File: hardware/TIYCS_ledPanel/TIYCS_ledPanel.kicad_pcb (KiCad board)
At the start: 2 copper layers, 203 x 203 mm, 120 parts

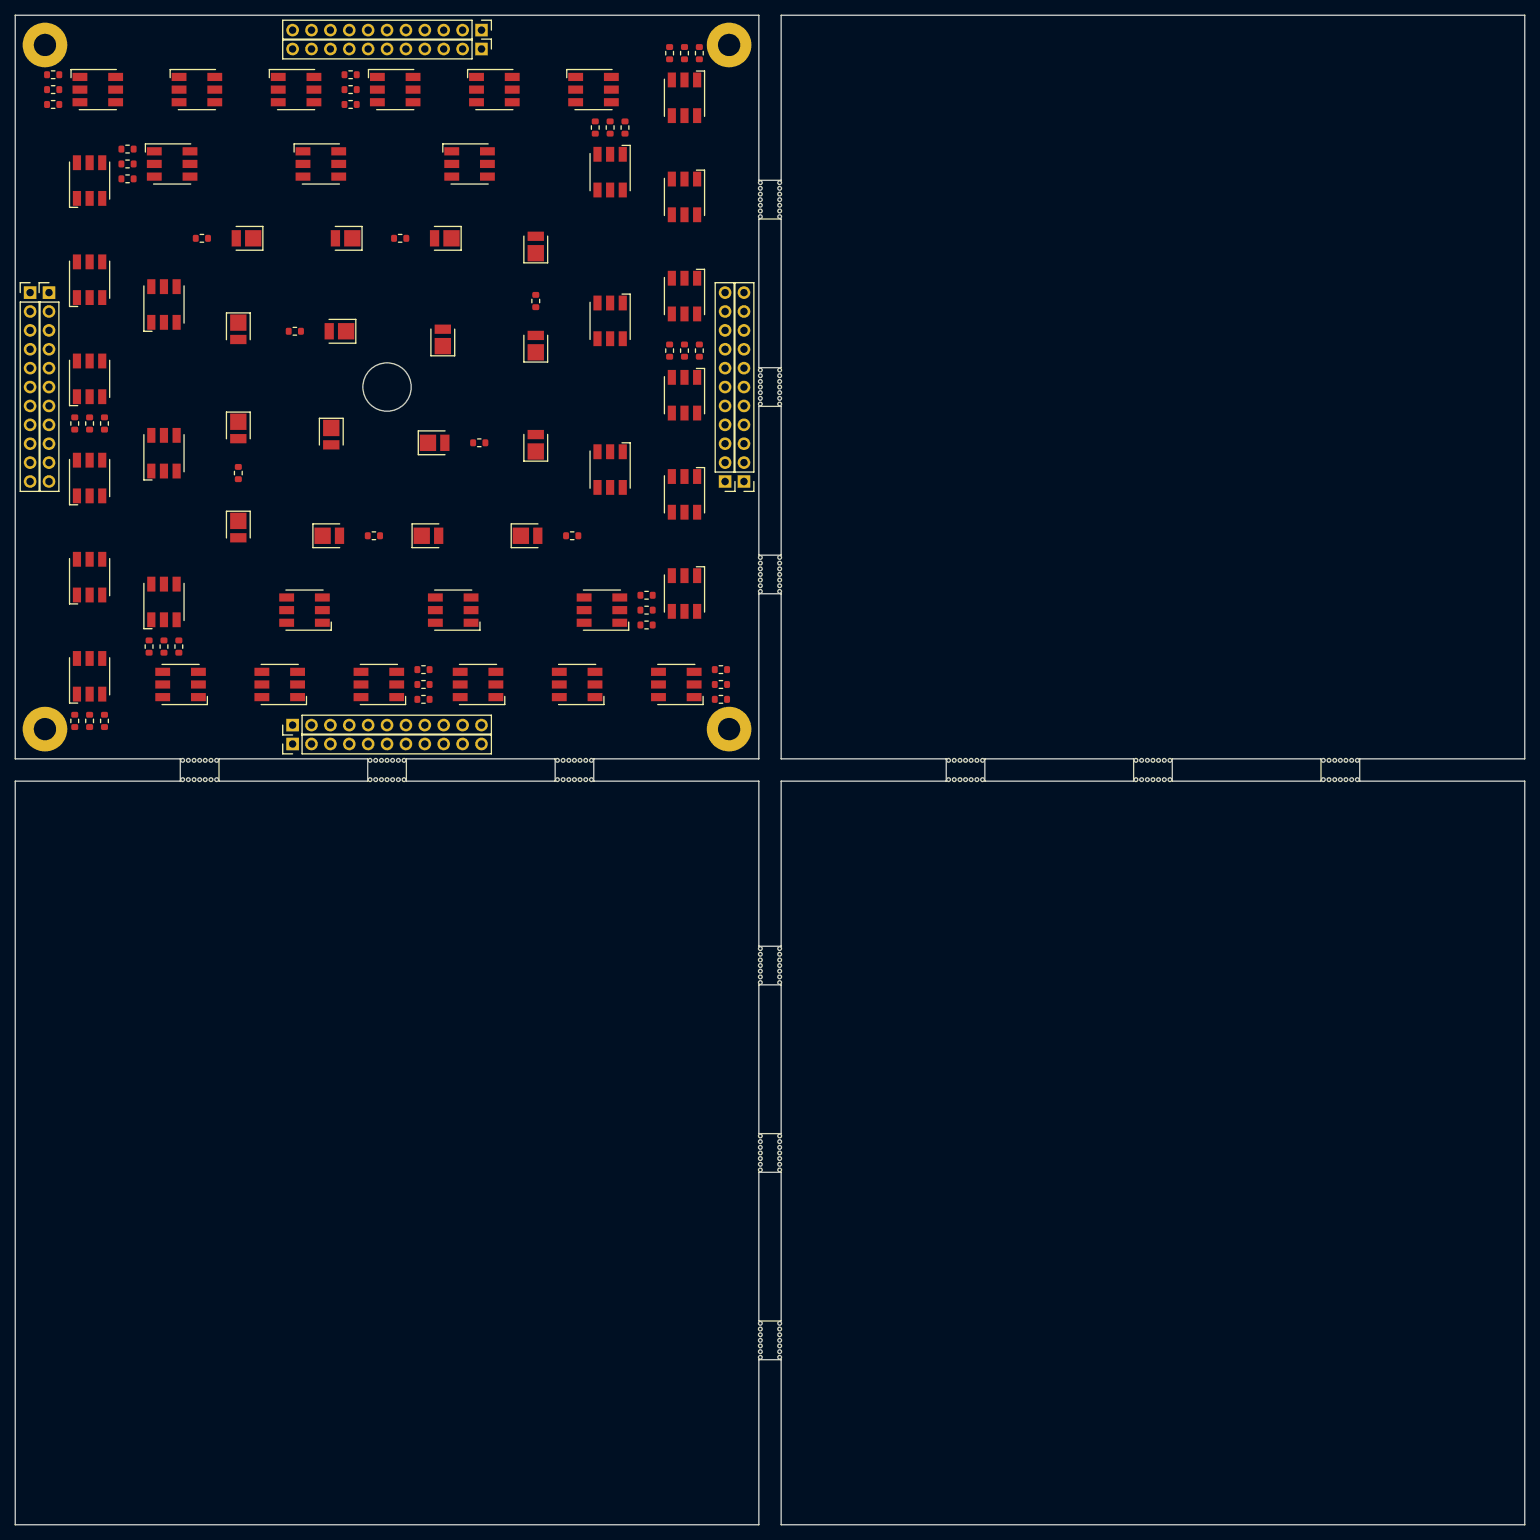
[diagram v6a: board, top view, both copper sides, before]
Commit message: PCLL-2 routed
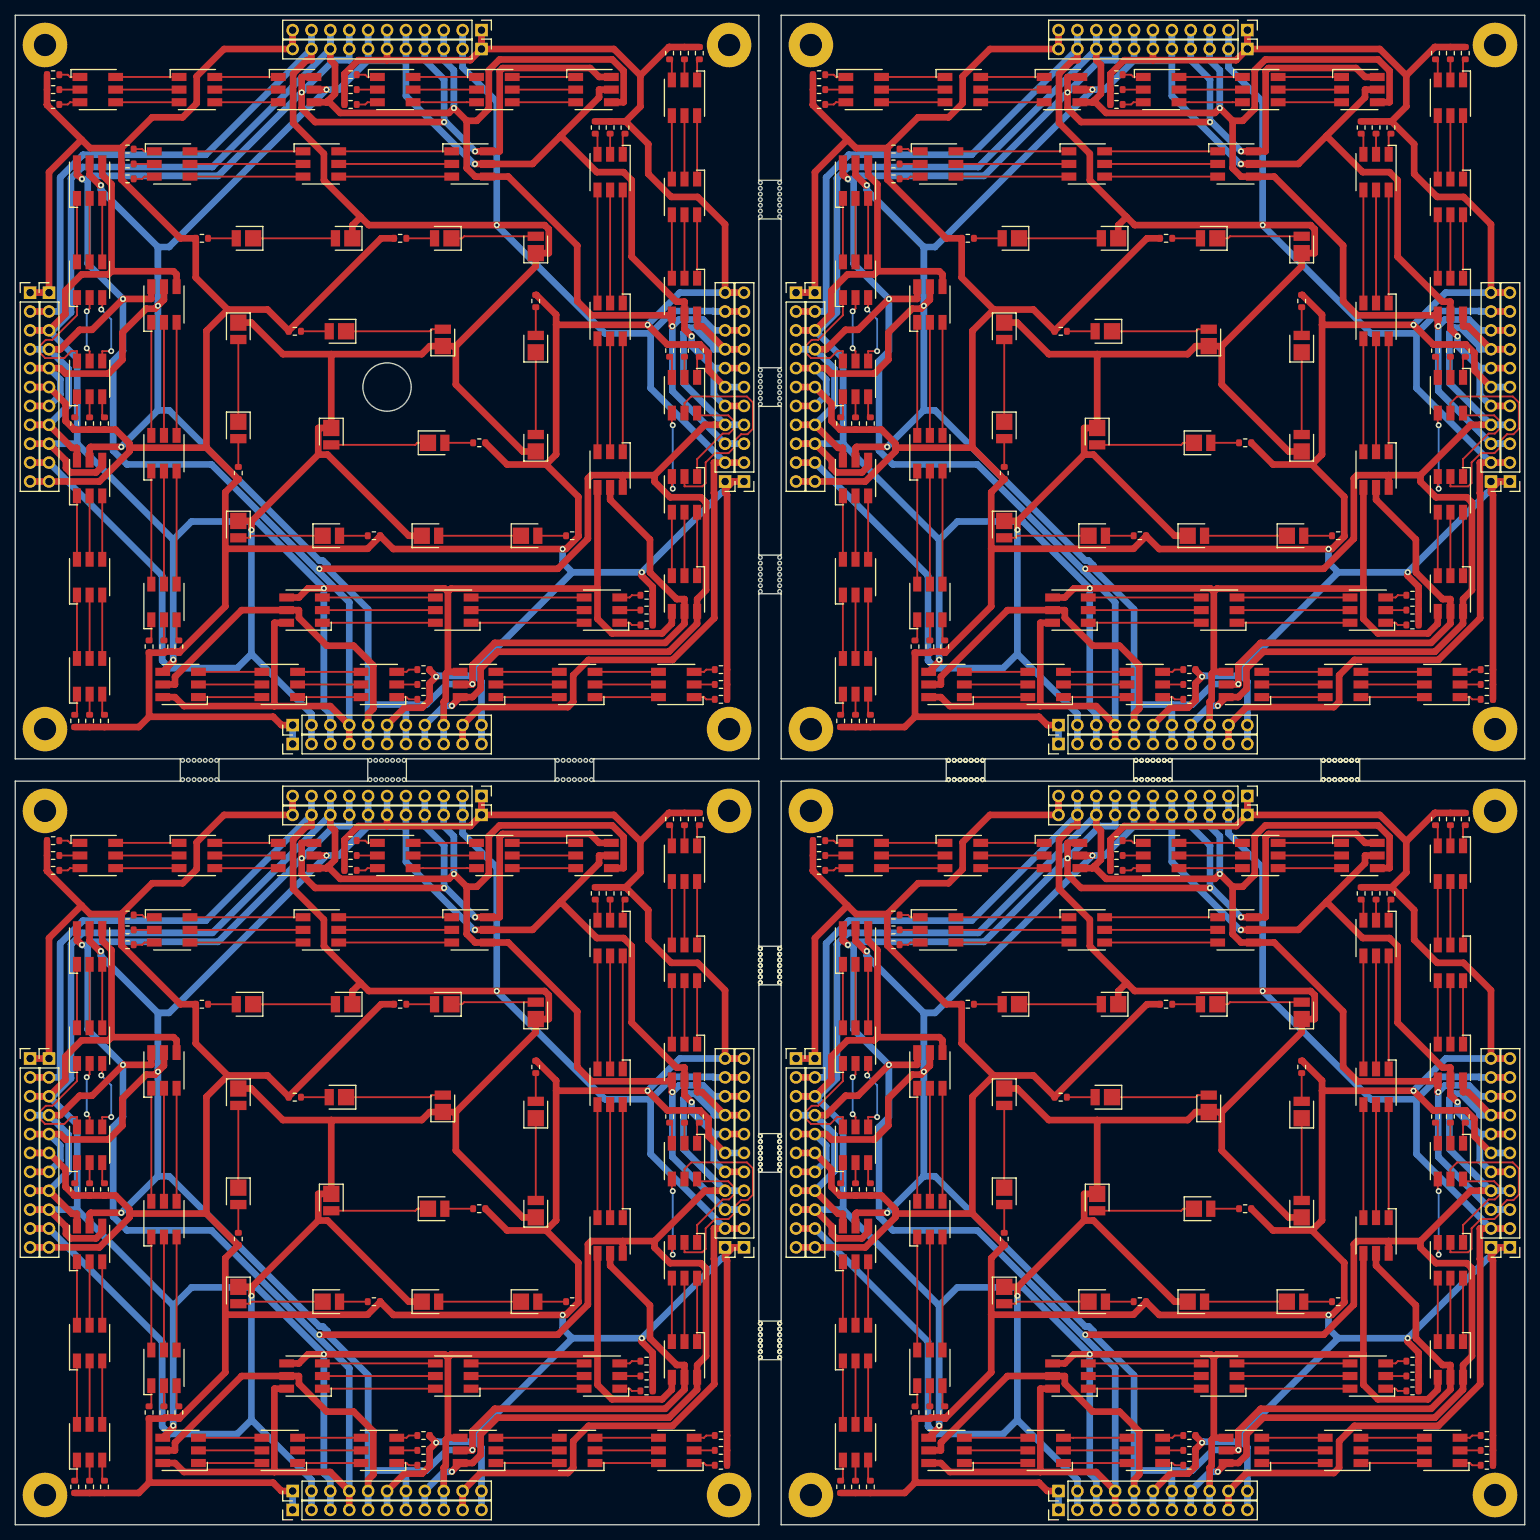
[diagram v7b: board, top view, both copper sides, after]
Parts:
- added H_10: MountingHole_3mm_Pad, MountingHole_3mm_Pad, F.Cu at (46.0, 149.0)
- added H_11: MountingHole_3mm_Pad, MountingHole_3mm_Pad, F.Cu at (-46.0, 149.0)
- added H_12: MountingHole_3mm_Pad, MountingHole_3mm_Pad, F.Cu at (57.0, 57.0)
- added H_13: MountingHole_3mm_Pad, MountingHole_3mm_Pad, F.Cu at (149.0, 57.0)
- added H_14: MountingHole_3mm_Pad, MountingHole_3mm_Pad, F.Cu at (149.0, 149.0)
- added H_15: MountingHole_3mm_Pad, MountingHole_3mm_Pad, F.Cu at (57.0, 149.0)
- added H_4: MountingHole_3mm_Pad, MountingHole_3mm_Pad, F.Cu at (57.0, -46.0)
- added H_5: MountingHole_3mm_Pad, MountingHole_3mm_Pad, F.Cu at (149.0, -46.0)
- added H_6: MountingHole_3mm_Pad, MountingHole_3mm_Pad, F.Cu at (149.0, 46.0)
- added H_7: MountingHole_3mm_Pad, MountingHole_3mm_Pad, F.Cu at (57.0, 46.0)
- added H_8: MountingHole_3mm_Pad, MountingHole_3mm_Pad, F.Cu at (-46.0, 57.0)
- added H_9: MountingHole_3mm_Pad, MountingHole_3mm_Pad, F.Cu at (46.0, 57.0)
- added LED_RGB2_12: LED_RGB_5050-6, LED_RGB_5050-6, F.Cu at (74.1, -30.0)
- added LED_RGB2_13: LED_RGB_5050-6, LED_RGB_5050-6, F.Cu at (94.1, -30.0)
- added LED_RGB2_14: LED_RGB_5050-6, LED_RGB_5050-6, F.Cu at (114.1, -30.0)
- added LED_RGB2_15: LED_RGB_5050-6, LED_RGB_5050-6, F.Cu at (133.0, -28.9)
- added LED_RGB2_16: LED_RGB_5050-6, LED_RGB_5050-6, F.Cu at (133.0, -8.90)
- added LED_RGB2_17: LED_RGB_5050-6, LED_RGB_5050-6, F.Cu at (133.0, 11.1)
- added LED_RGB2_18: LED_RGB_5050-6, LED_RGB_5050-6, F.Cu at (131.9, 30.0)
- added LED_RGB2_19: LED_RGB_5050-6, LED_RGB_5050-6, F.Cu at (111.9, 30.0)
- added LED_RGB2_20: LED_RGB_5050-6, LED_RGB_5050-6, F.Cu at (91.9, 30.0)
- added LED_RGB2_21: LED_RGB_5050-6, LED_RGB_5050-6, F.Cu at (73.0, 28.9)
- added LED_RGB2_22: LED_RGB_5050-6, LED_RGB_5050-6, F.Cu at (73.0, 8.90)
- added LED_RGB2_23: LED_RGB_5050-6, LED_RGB_5050-6, F.Cu at (73.0, -11.1)
- added LED_RGB2_24: LED_RGB_5050-6, LED_RGB_5050-6, F.Cu at (-28.9, 73.0)
- added LED_RGB2_25: LED_RGB_5050-6, LED_RGB_5050-6, F.Cu at (-8.90, 73.0)
- added LED_RGB2_26: LED_RGB_5050-6, LED_RGB_5050-6, F.Cu at (11.1, 73.0)
- added LED_RGB2_27: LED_RGB_5050-6, LED_RGB_5050-6, F.Cu at (30.0, 74.1)
- added LED_RGB2_28: LED_RGB_5050-6, LED_RGB_5050-6, F.Cu at (30.0, 94.1)
- added LED_RGB2_29: LED_RGB_5050-6, LED_RGB_5050-6, F.Cu at (30.0, 114.1)
- added LED_RGB2_30: LED_RGB_5050-6, LED_RGB_5050-6, F.Cu at (28.9, 133.0)
- added LED_RGB2_31: LED_RGB_5050-6, LED_RGB_5050-6, F.Cu at (8.90, 133.0)
- added LED_RGB2_32: LED_RGB_5050-6, LED_RGB_5050-6, F.Cu at (-11.1, 133.0)
- added LED_RGB2_33: LED_RGB_5050-6, LED_RGB_5050-6, F.Cu at (-30.0, 131.9)
- added LED_RGB2_34: LED_RGB_5050-6, LED_RGB_5050-6, F.Cu at (-30.0, 111.9)
- added LED_RGB2_35: LED_RGB_5050-6, LED_RGB_5050-6, F.Cu at (-30.0, 91.9)
- added LED_RGB2_36: LED_RGB_5050-6, LED_RGB_5050-6, F.Cu at (74.1, 73.0)
- added LED_RGB2_37: LED_RGB_5050-6, LED_RGB_5050-6, F.Cu at (94.1, 73.0)
- added LED_RGB2_38: LED_RGB_5050-6, LED_RGB_5050-6, F.Cu at (114.1, 73.0)
- added LED_RGB2_39: LED_RGB_5050-6, LED_RGB_5050-6, F.Cu at (133.0, 74.1)
- added LED_RGB2_40: LED_RGB_5050-6, LED_RGB_5050-6, F.Cu at (133.0, 94.1)
- added LED_RGB2_41: LED_RGB_5050-6, LED_RGB_5050-6, F.Cu at (133.0, 114.1)
- added LED_RGB2_42: LED_RGB_5050-6, LED_RGB_5050-6, F.Cu at (131.9, 133.0)
- added LED_RGB2_43: LED_RGB_5050-6, LED_RGB_5050-6, F.Cu at (111.9, 133.0)
- added LED_RGB2_44: LED_RGB_5050-6, LED_RGB_5050-6, F.Cu at (91.9, 133.0)
- added LED_RGB2_45: LED_RGB_5050-6, LED_RGB_5050-6, F.Cu at (73.0, 131.9)
- added LED_RGB2_46: LED_RGB_5050-6, LED_RGB_5050-6, F.Cu at (73.0, 111.9)
- added LED_RGB2_47: LED_RGB_5050-6, LED_RGB_5050-6, F.Cu at (73.0, 91.9)
- added LED_RGB_24: LED_RGB_5050-6, LED_RGB_5050-6, F.Cu at (64.1, -40.0)
- added LED_RGB_25: LED_RGB_5050-6, LED_RGB_5050-6, F.Cu at (77.4, -40.0)
- added LED_RGB_26: LED_RGB_5050-6, LED_RGB_5050-6, F.Cu at (90.8, -40.0)
- added LED_RGB_27: LED_RGB_5050-6, LED_RGB_5050-6, F.Cu at (104.1, -40.0)
- added LED_RGB_28: LED_RGB_5050-6, LED_RGB_5050-6, F.Cu at (117.4, -40.0)
- added LED_RGB_29: LED_RGB_5050-6, LED_RGB_5050-6, F.Cu at (130.8, -40.0)
- added LED_RGB_30: LED_RGB_5050-6, LED_RGB_5050-6, F.Cu at (143.0, -38.9)
- added LED_RGB_31: LED_RGB_5050-6, LED_RGB_5050-6, F.Cu at (143.0, -25.6)
- added LED_RGB_32: LED_RGB_5050-6, LED_RGB_5050-6, F.Cu at (143.0, -12.2)
- added LED_RGB_33: LED_RGB_5050-6, LED_RGB_5050-6, F.Cu at (143.0, 1.10)
- added LED_RGB_34: LED_RGB_5050-6, LED_RGB_5050-6, F.Cu at (143.0, 14.4)
- added LED_RGB_35: LED_RGB_5050-6, LED_RGB_5050-6, F.Cu at (143.0, 27.8)
- added LED_RGB_36: LED_RGB_5050-6, LED_RGB_5050-6, F.Cu at (141.9, 40.0)
- added LED_RGB_37: LED_RGB_5050-6, LED_RGB_5050-6, F.Cu at (128.6, 40.0)
- added LED_RGB_38: LED_RGB_5050-6, LED_RGB_5050-6, F.Cu at (115.2, 40.0)
- added LED_RGB_39: LED_RGB_5050-6, LED_RGB_5050-6, F.Cu at (101.9, 40.0)
- added LED_RGB_40: LED_RGB_5050-6, LED_RGB_5050-6, F.Cu at (88.6, 40.0)
- added LED_RGB_41: LED_RGB_5050-6, LED_RGB_5050-6, F.Cu at (75.2, 40.0)
- added LED_RGB_42: LED_RGB_5050-6, LED_RGB_5050-6, F.Cu at (63.0, 38.9)
- added LED_RGB_43: LED_RGB_5050-6, LED_RGB_5050-6, F.Cu at (63.0, 25.6)
- added LED_RGB_44: LED_RGB_5050-6, LED_RGB_5050-6, F.Cu at (63.0, 12.2)
- added LED_RGB_45: LED_RGB_5050-6, LED_RGB_5050-6, F.Cu at (63.0, -1.10)
- added LED_RGB_46: LED_RGB_5050-6, LED_RGB_5050-6, F.Cu at (63.0, -14.4)
- added LED_RGB_47: LED_RGB_5050-6, LED_RGB_5050-6, F.Cu at (63.0, -27.8)
- added LED_RGB_48: LED_RGB_5050-6, LED_RGB_5050-6, F.Cu at (-38.9, 63.0)
- added LED_RGB_49: LED_RGB_5050-6, LED_RGB_5050-6, F.Cu at (-25.6, 63.0)
- added LED_RGB_50: LED_RGB_5050-6, LED_RGB_5050-6, F.Cu at (-12.2, 63.0)
- added LED_RGB_51: LED_RGB_5050-6, LED_RGB_5050-6, F.Cu at (1.10, 63.0)
- added LED_RGB_52: LED_RGB_5050-6, LED_RGB_5050-6, F.Cu at (14.4, 63.0)
- added LED_RGB_53: LED_RGB_5050-6, LED_RGB_5050-6, F.Cu at (27.8, 63.0)
- added LED_RGB_54: LED_RGB_5050-6, LED_RGB_5050-6, F.Cu at (40.0, 64.1)
- added LED_RGB_55: LED_RGB_5050-6, LED_RGB_5050-6, F.Cu at (40.0, 77.4)
- added LED_RGB_56: LED_RGB_5050-6, LED_RGB_5050-6, F.Cu at (40.0, 90.8)
- added LED_RGB_57: LED_RGB_5050-6, LED_RGB_5050-6, F.Cu at (40.0, 104.1)
- added LED_RGB_58: LED_RGB_5050-6, LED_RGB_5050-6, F.Cu at (40.0, 117.4)
- added LED_RGB_59: LED_RGB_5050-6, LED_RGB_5050-6, F.Cu at (40.0, 130.8)
- added LED_RGB_60: LED_RGB_5050-6, LED_RGB_5050-6, F.Cu at (38.9, 143.0)
- added LED_RGB_61: LED_RGB_5050-6, LED_RGB_5050-6, F.Cu at (25.6, 143.0)
- added LED_RGB_62: LED_RGB_5050-6, LED_RGB_5050-6, F.Cu at (12.2, 143.0)
- added LED_RGB_63: LED_RGB_5050-6, LED_RGB_5050-6, F.Cu at (-1.10, 143.0)
- added LED_RGB_64: LED_RGB_5050-6, LED_RGB_5050-6, F.Cu at (-14.4, 143.0)
- added LED_RGB_65: LED_RGB_5050-6, LED_RGB_5050-6, F.Cu at (-27.8, 143.0)
- added LED_RGB_66: LED_RGB_5050-6, LED_RGB_5050-6, F.Cu at (-40.0, 141.9)
- added LED_RGB_67: LED_RGB_5050-6, LED_RGB_5050-6, F.Cu at (-40.0, 128.6)
- added LED_RGB_68: LED_RGB_5050-6, LED_RGB_5050-6, F.Cu at (-40.0, 115.2)
- added LED_RGB_69: LED_RGB_5050-6, LED_RGB_5050-6, F.Cu at (-40.0, 101.9)
- added LED_RGB_70: LED_RGB_5050-6, LED_RGB_5050-6, F.Cu at (-40.0, 88.6)
- added LED_RGB_71: LED_RGB_5050-6, LED_RGB_5050-6, F.Cu at (-40.0, 75.2)
- added LED_RGB_72: LED_RGB_5050-6, LED_RGB_5050-6, F.Cu at (64.1, 63.0)
- added LED_RGB_73: LED_RGB_5050-6, LED_RGB_5050-6, F.Cu at (77.4, 63.0)
- added LED_RGB_74: LED_RGB_5050-6, LED_RGB_5050-6, F.Cu at (90.8, 63.0)
- added LED_RGB_75: LED_RGB_5050-6, LED_RGB_5050-6, F.Cu at (104.1, 63.0)
- added LED_RGB_76: LED_RGB_5050-6, LED_RGB_5050-6, F.Cu at (117.4, 63.0)
- added LED_RGB_77: LED_RGB_5050-6, LED_RGB_5050-6, F.Cu at (130.8, 63.0)
- added LED_RGB_78: LED_RGB_5050-6, LED_RGB_5050-6, F.Cu at (143.0, 64.1)
- added LED_RGB_79: LED_RGB_5050-6, LED_RGB_5050-6, F.Cu at (143.0, 77.4)
- added LED_RGB_80: LED_RGB_5050-6, LED_RGB_5050-6, F.Cu at (143.0, 90.8)
- added LED_RGB_81: LED_RGB_5050-6, LED_RGB_5050-6, F.Cu at (143.0, 104.1)
- added LED_RGB_82: LED_RGB_5050-6, LED_RGB_5050-6, F.Cu at (143.0, 117.4)
- added LED_RGB_83: LED_RGB_5050-6, LED_RGB_5050-6, F.Cu at (143.0, 130.8)
- added LED_RGB_84: LED_RGB_5050-6, LED_RGB_5050-6, F.Cu at (141.9, 143.0)
- added LED_RGB_85: LED_RGB_5050-6, LED_RGB_5050-6, F.Cu at (128.6, 143.0)
- added LED_RGB_86: LED_RGB_5050-6, LED_RGB_5050-6, F.Cu at (115.2, 143.0)
- added LED_RGB_87: LED_RGB_5050-6, LED_RGB_5050-6, F.Cu at (101.9, 143.0)
- added LED_RGB_88: LED_RGB_5050-6, LED_RGB_5050-6, F.Cu at (88.6, 143.0)
- added LED_RGB_89: LED_RGB_5050-6, LED_RGB_5050-6, F.Cu at (75.2, 143.0)
- added LED_RGB_90: LED_RGB_5050-6, LED_RGB_5050-6, F.Cu at (63.0, 141.9)
- added LED_RGB_91: LED_RGB_5050-6, LED_RGB_5050-6, F.Cu at (63.0, 128.6)
- added LED_RGB_92: LED_RGB_5050-6, LED_RGB_5050-6, F.Cu at (63.0, 115.2)
- added LED_RGB_93: LED_RGB_5050-6, LED_RGB_5050-6, F.Cu at (63.0, 101.9)
- added LED_RGB_94: LED_RGB_5050-6, LED_RGB_5050-6, F.Cu at (63.0, 88.6)
- added LED_RGB_95: LED_RGB_5050-6, LED_RGB_5050-6, F.Cu at (63.0, 75.2)
- added LED_W2_10: LED_PLCC_2835, LED_PLCC_2835, F.Cu at (6.40, 110.5)
- added LED_W2_11: LED_PLCC_2835, LED_PLCC_2835, F.Cu at (-7.50, 109.4)
- added LED_W2_12: LED_PLCC_2835, LED_PLCC_2835, F.Cu at (96.6, 95.5)
- added LED_W2_13: LED_PLCC_2835, LED_PLCC_2835, F.Cu at (110.5, 96.6)
- added LED_W2_14: LED_PLCC_2835, LED_PLCC_2835, F.Cu at (109.4, 110.5)
- added LED_W2_15: LED_PLCC_2835, LED_PLCC_2835, F.Cu at (95.5, 109.4)
- added LED_W2_4: LED_PLCC_2835, LED_PLCC_2835, F.Cu at (96.6, -7.50)
- added LED_W2_5: LED_PLCC_2835, LED_PLCC_2835, F.Cu at (110.5, -6.40)
- added LED_W2_6: LED_PLCC_2835, LED_PLCC_2835, F.Cu at (109.4, 7.50)
- added LED_W2_7: LED_PLCC_2835, LED_PLCC_2835, F.Cu at (95.5, 6.40)
- added LED_W2_8: LED_PLCC_2835, LED_PLCC_2835, F.Cu at (-6.40, 95.5)
- added LED_W2_9: LED_PLCC_2835, LED_PLCC_2835, F.Cu at (7.50, 96.6)
- added LED_W_12: LED_PLCC_2835, LED_PLCC_2835, F.Cu at (84.1, -20.0)
- added LED_W_13: LED_PLCC_2835, LED_PLCC_2835, F.Cu at (97.4, -20.0)
- added LED_W_14: LED_PLCC_2835, LED_PLCC_2835, F.Cu at (110.8, -20.0)
- added LED_W_15: LED_PLCC_2835, LED_PLCC_2835, F.Cu at (123.0, -18.9)
- added LED_W_16: LED_PLCC_2835, LED_PLCC_2835, F.Cu at (123.0, -5.57)
- added LED_W_17: LED_PLCC_2835, LED_PLCC_2835, F.Cu at (123.0, 7.77)
- added LED_W_18: LED_PLCC_2835, LED_PLCC_2835, F.Cu at (121.9, 20.0)
- added LED_W_19: LED_PLCC_2835, LED_PLCC_2835, F.Cu at (108.6, 20.0)
- added LED_W_20: LED_PLCC_2835, LED_PLCC_2835, F.Cu at (95.2, 20.0)
- added LED_W_21: LED_PLCC_2835, LED_PLCC_2835, F.Cu at (83.0, 18.9)
- added LED_W_22: LED_PLCC_2835, LED_PLCC_2835, F.Cu at (83.0, 5.57)
- added LED_W_23: LED_PLCC_2835, LED_PLCC_2835, F.Cu at (83.0, -7.77)
- added LED_W_24: LED_PLCC_2835, LED_PLCC_2835, F.Cu at (-18.9, 83.0)
- added LED_W_25: LED_PLCC_2835, LED_PLCC_2835, F.Cu at (-5.57, 83.0)
- added LED_W_26: LED_PLCC_2835, LED_PLCC_2835, F.Cu at (7.77, 83.0)
- added LED_W_27: LED_PLCC_2835, LED_PLCC_2835, F.Cu at (20.0, 84.1)
- added LED_W_28: LED_PLCC_2835, LED_PLCC_2835, F.Cu at (20.0, 97.4)
- added LED_W_29: LED_PLCC_2835, LED_PLCC_2835, F.Cu at (20.0, 110.8)
- added LED_W_30: LED_PLCC_2835, LED_PLCC_2835, F.Cu at (18.9, 123.0)
- added LED_W_31: LED_PLCC_2835, LED_PLCC_2835, F.Cu at (5.57, 123.0)
- added LED_W_32: LED_PLCC_2835, LED_PLCC_2835, F.Cu at (-7.77, 123.0)
- added LED_W_33: LED_PLCC_2835, LED_PLCC_2835, F.Cu at (-20.0, 121.9)
- added LED_W_34: LED_PLCC_2835, LED_PLCC_2835, F.Cu at (-20.0, 108.6)
- added LED_W_35: LED_PLCC_2835, LED_PLCC_2835, F.Cu at (-20.0, 95.2)
- added LED_W_36: LED_PLCC_2835, LED_PLCC_2835, F.Cu at (84.1, 83.0)
- added LED_W_37: LED_PLCC_2835, LED_PLCC_2835, F.Cu at (97.4, 83.0)
- added LED_W_38: LED_PLCC_2835, LED_PLCC_2835, F.Cu at (110.8, 83.0)
- added LED_W_39: LED_PLCC_2835, LED_PLCC_2835, F.Cu at (123.0, 84.1)
- added LED_W_40: LED_PLCC_2835, LED_PLCC_2835, F.Cu at (123.0, 97.4)
- added LED_W_41: LED_PLCC_2835, LED_PLCC_2835, F.Cu at (123.0, 110.8)
- added LED_W_42: LED_PLCC_2835, LED_PLCC_2835, F.Cu at (121.9, 123.0)
- added LED_W_43: LED_PLCC_2835, LED_PLCC_2835, F.Cu at (108.6, 123.0)
- added LED_W_44: LED_PLCC_2835, LED_PLCC_2835, F.Cu at (95.2, 123.0)
- added LED_W_45: LED_PLCC_2835, LED_PLCC_2835, F.Cu at (83.0, 121.9)
- added LED_W_46: LED_PLCC_2835, LED_PLCC_2835, F.Cu at (83.0, 108.6)
- added LED_W_47: LED_PLCC_2835, LED_PLCC_2835, F.Cu at (83.0, 95.2)
- added R_0_0_RGB1: R_0603_1608Metric, R_0603_1608Metric, F.Cu at (58.1, -40.0)
- added R_0_0_RGB3: R_0603_1608Metric, R_0603_1608Metric, F.Cu at (68.1, -30.0)
- added R_0_0_RGB4: R_0603_1608Metric, R_0603_1608Metric, F.Cu at (-44.9, 63.0)
- added R_0_0_RGB5: R_0603_1608Metric, R_0603_1608Metric, F.Cu at (-34.9, 73.0)
- added R_0_0_RGB6: R_0603_1608Metric, R_0603_1608Metric, F.Cu at (58.1, 63.0)
- added R_0_0_RGB7: R_0603_1608Metric, R_0603_1608Metric, F.Cu at (68.1, 73.0)
- added R_0_0_W1: R_0603_1608Metric, R_0603_1608Metric, F.Cu at (78.1, -20.0)
- added R_0_0_W3: R_0603_1608Metric, R_0603_1608Metric, F.Cu at (90.6, -7.50)
- added R_0_0_W4: R_0603_1608Metric, R_0603_1608Metric, F.Cu at (-24.9, 83.0)
- added R_0_0_W5: R_0603_1608Metric, R_0603_1608Metric, F.Cu at (-12.4, 95.5)
- added R_0_0_W6: R_0603_1608Metric, R_0603_1608Metric, F.Cu at (78.1, 83.0)
- added R_0_0_W7: R_0603_1608Metric, R_0603_1608Metric, F.Cu at (90.6, 95.5)
- added R_0_1_RGB1: R_0603_1608Metric, R_0603_1608Metric, F.Cu at (58.1, -42.0)
- added R_0_1_RGB3: R_0603_1608Metric, R_0603_1608Metric, F.Cu at (68.1, -32.0)
- added R_0_1_RGB4: R_0603_1608Metric, R_0603_1608Metric, F.Cu at (-44.9, 61.0)
- added R_0_1_RGB5: R_0603_1608Metric, R_0603_1608Metric, F.Cu at (-34.9, 71.0)
- added R_0_1_RGB6: R_0603_1608Metric, R_0603_1608Metric, F.Cu at (58.1, 61.0)
- added R_0_1_RGB7: R_0603_1608Metric, R_0603_1608Metric, F.Cu at (68.1, 71.0)
- added R_0_2_RGB1: R_0603_1608Metric, R_0603_1608Metric, F.Cu at (58.1, -38.0)
- added R_0_2_RGB3: R_0603_1608Metric, R_0603_1608Metric, F.Cu at (68.1, -28.0)
- added R_0_2_RGB4: R_0603_1608Metric, R_0603_1608Metric, F.Cu at (-44.9, 65.0)
- added R_0_2_RGB5: R_0603_1608Metric, R_0603_1608Metric, F.Cu at (-34.9, 75.0)
- added R_0_2_RGB6: R_0603_1608Metric, R_0603_1608Metric, F.Cu at (58.1, 65.0)
- added R_0_2_RGB7: R_0603_1608Metric, R_0603_1608Metric, F.Cu at (68.1, 75.0)
- added R_10_0_W1: R_0603_1608Metric, R_0603_1608Metric, F.Cu at (83.0, 11.6)
- added R_10_0_W2: R_0603_1608Metric, R_0603_1608Metric, F.Cu at (-20.0, 114.6)
- added R_10_0_W3: R_0603_1608Metric, R_0603_1608Metric, F.Cu at (83.0, 114.6)
- added R_12_0_RGB1: R_0603_1608Metric, R_0603_1608Metric, F.Cu at (147.9, 40.0)
- added R_12_0_RGB2: R_0603_1608Metric, R_0603_1608Metric, F.Cu at (44.9, 143.0)
- added R_12_0_RGB3: R_0603_1608Metric, R_0603_1608Metric, F.Cu at (147.9, 143.0)
- added R_12_1_RGB1: R_0603_1608Metric, R_0603_1608Metric, F.Cu at (147.9, 42.0)
- added R_12_1_RGB2: R_0603_1608Metric, R_0603_1608Metric, F.Cu at (44.9, 145.0)
- added R_12_1_RGB3: R_0603_1608Metric, R_0603_1608Metric, F.Cu at (147.9, 145.0)
- added R_12_2_RGB1: R_0603_1608Metric, R_0603_1608Metric, F.Cu at (147.9, 38.0)
- added R_12_2_RGB2: R_0603_1608Metric, R_0603_1608Metric, F.Cu at (44.9, 141.0)
- added R_12_2_RGB3: R_0603_1608Metric, R_0603_1608Metric, F.Cu at (147.9, 141.0)
- added R_15_0_RGB1: R_0603_1608Metric, R_0603_1608Metric, F.Cu at (107.9, 40.0)
- added R_15_0_RGB2: R_0603_1608Metric, R_0603_1608Metric, F.Cu at (4.90, 143.0)
- added R_15_0_RGB3: R_0603_1608Metric, R_0603_1608Metric, F.Cu at (107.9, 143.0)
- added R_15_1_RGB1: R_0603_1608Metric, R_0603_1608Metric, F.Cu at (107.9, 42.0)
- added R_15_1_RGB2: R_0603_1608Metric, R_0603_1608Metric, F.Cu at (4.90, 145.0)
- added R_15_1_RGB3: R_0603_1608Metric, R_0603_1608Metric, F.Cu at (107.9, 145.0)
- added R_15_2_RGB1: R_0603_1608Metric, R_0603_1608Metric, F.Cu at (107.9, 38.0)
- added R_15_2_RGB2: R_0603_1608Metric, R_0603_1608Metric, F.Cu at (4.90, 141.0)
- added R_15_2_RGB3: R_0603_1608Metric, R_0603_1608Metric, F.Cu at (107.9, 141.0)
- added R_18_0_RGB1: R_0603_1608Metric, R_0603_1608Metric, F.Cu at (63.0, 44.9)
- added R_18_0_RGB2: R_0603_1608Metric, R_0603_1608Metric, F.Cu at (-40.0, 147.9)
- added R_18_0_RGB3: R_0603_1608Metric, R_0603_1608Metric, F.Cu at (63.0, 147.9)
- added R_18_1_RGB1: R_0603_1608Metric, R_0603_1608Metric, F.Cu at (61.0, 44.9)
- added R_18_1_RGB2: R_0603_1608Metric, R_0603_1608Metric, F.Cu at (-42.0, 147.9)
- added R_18_1_RGB3: R_0603_1608Metric, R_0603_1608Metric, F.Cu at (61.0, 147.9)
- added R_18_2_RGB1: R_0603_1608Metric, R_0603_1608Metric, F.Cu at (65.0, 44.9)
- added R_18_2_RGB2: R_0603_1608Metric, R_0603_1608Metric, F.Cu at (-38.0, 147.9)
- added R_18_2_RGB3: R_0603_1608Metric, R_0603_1608Metric, F.Cu at (65.0, 147.9)
- added R_21_0_RGB1: R_0603_1608Metric, R_0603_1608Metric, F.Cu at (63.0, 4.90)
- added R_21_0_RGB2: R_0603_1608Metric, R_0603_1608Metric, F.Cu at (-40.0, 107.9)
- added R_21_0_RGB3: R_0603_1608Metric, R_0603_1608Metric, F.Cu at (63.0, 107.9)
- added R_21_1_RGB1: R_0603_1608Metric, R_0603_1608Metric, F.Cu at (61.0, 4.90)
- added R_21_1_RGB2: R_0603_1608Metric, R_0603_1608Metric, F.Cu at (-42.0, 107.9)
- added R_21_1_RGB3: R_0603_1608Metric, R_0603_1608Metric, F.Cu at (61.0, 107.9)
- added R_21_2_RGB1: R_0603_1608Metric, R_0603_1608Metric, F.Cu at (65.0, 4.90)
- added R_21_2_RGB2: R_0603_1608Metric, R_0603_1608Metric, F.Cu at (-38.0, 107.9)
- added R_21_2_RGB3: R_0603_1608Metric, R_0603_1608Metric, F.Cu at (65.0, 107.9)
- added R_2_0_W1: R_0603_1608Metric, R_0603_1608Metric, F.Cu at (104.8, -20.0)
- added R_2_0_W3: R_0603_1608Metric, R_0603_1608Metric, F.Cu at (115.4, 7.50)
- added R_2_0_W4: R_0603_1608Metric, R_0603_1608Metric, F.Cu at (1.77, 83.0)
- added R_2_0_W5: R_0603_1608Metric, R_0603_1608Metric, F.Cu at (12.4, 110.5)
- added R_2_0_W6: R_0603_1608Metric, R_0603_1608Metric, F.Cu at (104.8, 83.0)
- added R_2_0_W7: R_0603_1608Metric, R_0603_1608Metric, F.Cu at (115.4, 110.5)
- added R_3_0_RGB1: R_0603_1608Metric, R_0603_1608Metric, F.Cu at (98.1, -40.0)
- added R_3_0_RGB3: R_0603_1608Metric, R_0603_1608Metric, F.Cu at (133.0, -34.9)
- added R_3_0_RGB4: R_0603_1608Metric, R_0603_1608Metric, F.Cu at (-4.90, 63.0)
- added R_3_0_RGB5: R_0603_1608Metric, R_0603_1608Metric, F.Cu at (30.0, 68.1)
- added R_3_0_RGB6: R_0603_1608Metric, R_0603_1608Metric, F.Cu at (98.1, 63.0)
- added R_3_0_RGB7: R_0603_1608Metric, R_0603_1608Metric, F.Cu at (133.0, 68.1)
- added R_3_1_RGB1: R_0603_1608Metric, R_0603_1608Metric, F.Cu at (98.1, -42.0)
- added R_3_1_RGB3: R_0603_1608Metric, R_0603_1608Metric, F.Cu at (135.0, -34.9)
- added R_3_1_RGB4: R_0603_1608Metric, R_0603_1608Metric, F.Cu at (-4.90, 61.0)
- added R_3_1_RGB5: R_0603_1608Metric, R_0603_1608Metric, F.Cu at (32.0, 68.1)
- added R_3_1_RGB6: R_0603_1608Metric, R_0603_1608Metric, F.Cu at (98.1, 61.0)
- added R_3_1_RGB7: R_0603_1608Metric, R_0603_1608Metric, F.Cu at (135.0, 68.1)
- added R_3_2_RGB1: R_0603_1608Metric, R_0603_1608Metric, F.Cu at (98.1, -38.0)
- added R_3_2_RGB3: R_0603_1608Metric, R_0603_1608Metric, F.Cu at (131.0, -34.9)
- added R_3_2_RGB4: R_0603_1608Metric, R_0603_1608Metric, F.Cu at (-4.90, 65.0)
- added R_3_2_RGB5: R_0603_1608Metric, R_0603_1608Metric, F.Cu at (28.0, 68.1)
- added R_3_2_RGB6: R_0603_1608Metric, R_0603_1608Metric, F.Cu at (98.1, 65.0)
- added R_3_2_RGB7: R_0603_1608Metric, R_0603_1608Metric, F.Cu at (131.0, 68.1)
- added R_4_0_W1: R_0603_1608Metric, R_0603_1608Metric, F.Cu at (123.0, -11.6)
- added R_4_0_W2: R_0603_1608Metric, R_0603_1608Metric, F.Cu at (20.0, 91.4)
- added R_4_0_W3: R_0603_1608Metric, R_0603_1608Metric, F.Cu at (123.0, 91.4)
- added R_6_0_RGB1: R_0603_1608Metric, R_0603_1608Metric, F.Cu at (143.0, -44.9)
- added R_6_0_RGB3: R_0603_1608Metric, R_0603_1608Metric, F.Cu at (137.9, 30.0)
- added R_6_0_RGB4: R_0603_1608Metric, R_0603_1608Metric, F.Cu at (40.0, 58.1)
- added R_6_0_RGB5: R_0603_1608Metric, R_0603_1608Metric, F.Cu at (34.9, 133.0)
- added R_6_0_RGB6: R_0603_1608Metric, R_0603_1608Metric, F.Cu at (143.0, 58.1)
- added R_6_0_RGB7: R_0603_1608Metric, R_0603_1608Metric, F.Cu at (137.9, 133.0)
- added R_6_0_W1: R_0603_1608Metric, R_0603_1608Metric, F.Cu at (127.9, 20.0)
- added R_6_0_W2: R_0603_1608Metric, R_0603_1608Metric, F.Cu at (24.9, 123.0)
- added R_6_0_W3: R_0603_1608Metric, R_0603_1608Metric, F.Cu at (127.9, 123.0)
- added R_6_1_RGB1: R_0603_1608Metric, R_0603_1608Metric, F.Cu at (145.0, -44.9)
- added R_6_1_RGB3: R_0603_1608Metric, R_0603_1608Metric, F.Cu at (137.9, 32.0)
- added R_6_1_RGB4: R_0603_1608Metric, R_0603_1608Metric, F.Cu at (42.0, 58.1)
- added R_6_1_RGB5: R_0603_1608Metric, R_0603_1608Metric, F.Cu at (34.9, 135.0)
- added R_6_1_RGB6: R_0603_1608Metric, R_0603_1608Metric, F.Cu at (145.0, 58.1)
- added R_6_1_RGB7: R_0603_1608Metric, R_0603_1608Metric, F.Cu at (137.9, 135.0)
- added R_6_2_RGB1: R_0603_1608Metric, R_0603_1608Metric, F.Cu at (141.0, -44.9)
- added R_6_2_RGB3: R_0603_1608Metric, R_0603_1608Metric, F.Cu at (137.9, 28.0)
- added R_6_2_RGB4: R_0603_1608Metric, R_0603_1608Metric, F.Cu at (38.0, 58.1)
- added R_6_2_RGB5: R_0603_1608Metric, R_0603_1608Metric, F.Cu at (34.9, 131.0)
- added R_6_2_RGB6: R_0603_1608Metric, R_0603_1608Metric, F.Cu at (141.0, 58.1)
- added R_6_2_RGB7: R_0603_1608Metric, R_0603_1608Metric, F.Cu at (137.9, 131.0)
- added R_8_0_W1: R_0603_1608Metric, R_0603_1608Metric, F.Cu at (101.2, 20.0)
- added R_8_0_W2: R_0603_1608Metric, R_0603_1608Metric, F.Cu at (-1.77, 123.0)
- added R_8_0_W3: R_0603_1608Metric, R_0603_1608Metric, F.Cu at (101.2, 123.0)
- added R_9_0_RGB1: R_0603_1608Metric, R_0603_1608Metric, F.Cu at (143.0, -4.90)
- added R_9_0_RGB3: R_0603_1608Metric, R_0603_1608Metric, F.Cu at (73.0, 34.9)
- added R_9_0_RGB4: R_0603_1608Metric, R_0603_1608Metric, F.Cu at (40.0, 98.1)
- added R_9_0_RGB5: R_0603_1608Metric, R_0603_1608Metric, F.Cu at (-30.0, 137.9)
- added R_9_0_RGB6: R_0603_1608Metric, R_0603_1608Metric, F.Cu at (143.0, 98.1)
- added R_9_0_RGB7: R_0603_1608Metric, R_0603_1608Metric, F.Cu at (73.0, 137.9)
- added R_9_1_RGB1: R_0603_1608Metric, R_0603_1608Metric, F.Cu at (145.0, -4.90)
- added R_9_1_RGB3: R_0603_1608Metric, R_0603_1608Metric, F.Cu at (71.0, 34.9)
- added R_9_1_RGB4: R_0603_1608Metric, R_0603_1608Metric, F.Cu at (42.0, 98.1)
- added R_9_1_RGB5: R_0603_1608Metric, R_0603_1608Metric, F.Cu at (-32.0, 137.9)
- added R_9_1_RGB6: R_0603_1608Metric, R_0603_1608Metric, F.Cu at (145.0, 98.1)
- added R_9_1_RGB7: R_0603_1608Metric, R_0603_1608Metric, F.Cu at (71.0, 137.9)
- added R_9_2_RGB1: R_0603_1608Metric, R_0603_1608Metric, F.Cu at (141.0, -4.90)
- added R_9_2_RGB3: R_0603_1608Metric, R_0603_1608Metric, F.Cu at (75.0, 34.9)
- added R_9_2_RGB4: R_0603_1608Metric, R_0603_1608Metric, F.Cu at (38.0, 98.1)
- added R_9_2_RGB5: R_0603_1608Metric, R_0603_1608Metric, F.Cu at (-28.0, 137.9)
- added R_9_2_RGB6: R_0603_1608Metric, R_0603_1608Metric, F.Cu at (141.0, 98.1)
- added R_9_2_RGB7: R_0603_1608Metric, R_0603_1608Metric, F.Cu at (75.0, 137.9)
- added mainConn_0_2: PinHeader_1x11_P2.54mm_Vertical, PinHeader_1x11_P2.54mm_Vertical, F.Cu at (55.0, -12.7)
- added mainConn_0_3: PinHeader_1x11_P2.54mm_Vertical, PinHeader_1x11_P2.54mm_Vertical, F.Cu at (57.5, -12.7)
- added mainConn_0_4: PinHeader_1x11_P2.54mm_Vertical, PinHeader_1x11_P2.54mm_Vertical, F.Cu at (-48.0, 90.3)
- added mainConn_0_5: PinHeader_1x11_P2.54mm_Vertical, PinHeader_1x11_P2.54mm_Vertical, F.Cu at (-45.5, 90.3)
- added mainConn_0_6: PinHeader_1x11_P2.54mm_Vertical, PinHeader_1x11_P2.54mm_Vertical, F.Cu at (55.0, 90.3)
- added mainConn_0_7: PinHeader_1x11_P2.54mm_Vertical, PinHeader_1x11_P2.54mm_Vertical, F.Cu at (57.5, 90.3)
- added mainConn_1_2: PinHeader_1x11_P2.54mm_Vertical, PinHeader_1x11_P2.54mm_Vertical, F.Cu at (115.7, -48.0)
- added mainConn_1_3: PinHeader_1x11_P2.54mm_Vertical, PinHeader_1x11_P2.54mm_Vertical, F.Cu at (115.7, -45.5)
- added mainConn_1_4: PinHeader_1x11_P2.54mm_Vertical, PinHeader_1x11_P2.54mm_Vertical, F.Cu at (12.7, 55.0)
- added mainConn_1_5: PinHeader_1x11_P2.54mm_Vertical, PinHeader_1x11_P2.54mm_Vertical, F.Cu at (12.7, 57.5)
- added mainConn_1_6: PinHeader_1x11_P2.54mm_Vertical, PinHeader_1x11_P2.54mm_Vertical, F.Cu at (115.7, 55.0)
- added mainConn_1_7: PinHeader_1x11_P2.54mm_Vertical, PinHeader_1x11_P2.54mm_Vertical, F.Cu at (115.7, 57.5)
- added mainConn_2_2: PinHeader_1x11_P2.54mm_Vertical, PinHeader_1x11_P2.54mm_Vertical, F.Cu at (151.0, 12.7)
- added mainConn_2_3: PinHeader_1x11_P2.54mm_Vertical, PinHeader_1x11_P2.54mm_Vertical, F.Cu at (148.5, 12.7)
- added mainConn_2_4: PinHeader_1x11_P2.54mm_Vertical, PinHeader_1x11_P2.54mm_Vertical, F.Cu at (48.0, 115.7)
- added mainConn_2_5: PinHeader_1x11_P2.54mm_Vertical, PinHeader_1x11_P2.54mm_Vertical, F.Cu at (45.5, 115.7)
- added mainConn_2_6: PinHeader_1x11_P2.54mm_Vertical, PinHeader_1x11_P2.54mm_Vertical, F.Cu at (151.0, 115.7)
- added mainConn_2_7: PinHeader_1x11_P2.54mm_Vertical, PinHeader_1x11_P2.54mm_Vertical, F.Cu at (148.5, 115.7)
- added mainConn_3_2: PinHeader_1x11_P2.54mm_Vertical, PinHeader_1x11_P2.54mm_Vertical, F.Cu at (90.3, 48.0)
- added mainConn_3_3: PinHeader_1x11_P2.54mm_Vertical, PinHeader_1x11_P2.54mm_Vertical, F.Cu at (90.3, 45.5)
- added mainConn_3_4: PinHeader_1x11_P2.54mm_Vertical, PinHeader_1x11_P2.54mm_Vertical, F.Cu at (-12.7, 151.0)
- added mainConn_3_5: PinHeader_1x11_P2.54mm_Vertical, PinHeader_1x11_P2.54mm_Vertical, F.Cu at (-12.7, 148.5)
- added mainConn_3_6: PinHeader_1x11_P2.54mm_Vertical, PinHeader_1x11_P2.54mm_Vertical, F.Cu at (90.3, 151.0)
- added mainConn_3_7: PinHeader_1x11_P2.54mm_Vertical, PinHeader_1x11_P2.54mm_Vertical, F.Cu at (90.3, 148.5)
- added mouseBite_184: mouseBiteCustom, mouseBiteCustom, F.Cu at (128.2, 51.5)
- added mouseBite_605: mouseBiteCustom, mouseBiteCustom, F.Cu at (51.5, 128.2)
- added mouseBite_609: mouseBiteCustom, mouseBiteCustom, F.Cu at (103.0, 51.5)
- added mouseBite_66: mouseBiteCustom, mouseBiteCustom, F.Cu at (77.8, 51.5)
- added mouseBite_695: mouseBiteCustom, mouseBiteCustom, F.Cu at (51.5, 103.0)
- added mouseBite_754: mouseBiteCustom, mouseBiteCustom, F.Cu at (51.5, 77.8)
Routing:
- net 12V: track 0.00 -> 2551.6 mm, vias 0 -> 16
- net W: track 0.00 -> 1941.7 mm, vias 0 -> 8
- net G: track 0.00 -> 1917.6 mm, vias 0 -> 28
- net B: track 0.00 -> 1902.6 mm, vias 0 -> 16
- net R: track 0.00 -> 1664.3 mm, vias 0 -> 28
- net D9toD10_Red_1: track 0.00 -> 122.5 mm
- net D21toD22_Green_1: track 0.00 -> 67.8 mm
- net D9toD10_Green_1: track 0.00 -> 61.6 mm
- net D9toD10_Blue_2: track 0.00 -> 60.8 mm
- net D6toD7_Red_2: track 0.00 -> 60.8 mm
- net D6toD7_Green_2: track 0.00 -> 60.8 mm
- net D6toD7_Blue_2: track 0.00 -> 60.8 mm
- net D4toD5_Green_2: track 0.00 -> 60.8 mm
- net D3toD4_Red_2: track 0.00 -> 60.8 mm
- net D3toD4_Blue_2: track 0.00 -> 60.8 mm
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
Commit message: Ordered hardware
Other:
- outline, holes or cut-outs redrawn
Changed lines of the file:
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@@
       (outputformat 1)
       (mirror false)
-      (drillshape 1)
+      (drillshape 0)
       (scaleselection 1)
       (outputdirectory "")
@@
     (fp_line (start 1.75 -1.4) (end 1.75 1.4) (layer "F.Fab") (width 0.1))
     (fp_line (start -1.75 1.4) (end -1.75 -0.7) (layer "F.Fab") (width 0.1))
-    (fp_line (start -1.05 -1.4) (end 1.75 -1.4) (layer "F.Fab") (width 0.1))
     (fp_line (start 1.75 1.4) (end -1.75 1.4) (layer "F.Fab") (width 0.1))
+    (fp_line (start -1.05 -1.4) (end 1.75 -1.4) (layer "F.Fab") (width 0.1))
     (pad "1" smd rect locked (at -0.9 0 180) (size 2.2 2.2) (layers "F.Cu" "F.Paste" "F.Mask")
       (net 5 "W"))
@@
     (fp_line (start 2.5 2.7) (end -2.5 2.7) (layer "F.SilkS") (width 0.12))
     (fp_line (start -3.6 -2.7) (end 2.5 -2.7) (layer "F.SilkS") (width 0.12))
-    (fp_line (start 3.65 2.75) (end 3.65 -2.75) (layer "F.CrtYd") (width 0.05))
     (fp_line (start -3.65 2.75) (end 3.65 2.75) (layer "F.CrtYd") (width 0.05))
     (fp_line (start -3.65 -2.75) (end -3.65 2.75) (layer "F.CrtYd") (width 0.05))
+    (fp_line (start 3.65 2.75) (end 3.65 -2.75) (layer "F.CrtYd") (width 0.05))
     (fp_line (start 3.65 -2.75) (end -3.65 -2.75) (layer "F.CrtYd") (width 0.05))
+    (fp_line (start -2.5 -2.5) (end -2.5 2.5) (layer "F.Fab") (width 0.1))
     (fp_line (start -2.5 -1.9) (end -1.9 -2.5) (layer "F.Fab") (width 0.1))
     (fp_line (start -2.5 2.5) (end 2.5 2.5) (layer "F.Fab") (width 0.1))
-    (fp_line (start 2.5 2.5) (end 2.5 -2.5) (layer "F.Fab") (width 0.1))
     (fp_line (start 2.5 -2.5) (end -2.5 -2.5) (layer "F.Fab") (width 0.1))
-    (fp_line (start -2.5 -2.5) (end -2.5 2.5) (layer "F.Fab") (width 0.1))
+    (fp_line (start 2.5 2.5) (end 2.5 -2.5) (layer "F.Fab") (width 0.1))
     (fp_circle (center 0 0) (end 0 -1.9) (layer "F.Fab") (width 0.1) (fill none))
     (pad "1" smd rect locked (at -2.4 -1.7) (size 1.1 2) (layers "F.Cu" "F.Paste" "F.Mask")
@@
   (gr_line (start -50 153) (end 50 153) (layer "Edge.Cuts") (width 0.1))
   (gr_line (start 53 -50) (end 53 -27.799999) (layer "Edge.Cuts") (width 0.1))
+  (gr_circle (center 0 0) (end 3.25 0) (layer "Edge.Cuts") (width 0.1) (fill none))
   (gr_line (start 50 53) (end 50 75.2) (layer "Edge.Cuts") (width 0.1))
   (gr_line (start 50 2.6) (end 53 2.6) (layer "Edge.Cuts") (width 0.1))
@@
   (gr_line (start 50 80.4) (end 53 80.4) (layer "Edge.Cuts") (width 0.1))
   (gr_line (start -50 -50) (end -50 50) (layer "Edge.Cuts") (width 0.1))
+  (gr_circle (center 0 103) (end 3.25 103) (layer "Edge.Cuts") (width 0.1) (fill none))
   (gr_line (start 53 50) (end 75.2 50) (layer "Edge.Cuts") (width 0.1))
   (gr_line (start 80.4 53) (end 100.4 53) (layer "Edge.Cuts") (width 0.1))
@@
   (gr_line (start 50 -27.799999) (end 53 -27.799999) (layer "Edge.Cuts") (width 0.1))
   (gr_line (start 50 130.799999) (end 53 130.799999) (layer "Edge.Cuts") (width 0.1))
+  (gr_circle (center 103 103) (end 106.25 103) (layer "Edge.Cuts") (width 0.1) (fill none))
   (gr_line (start 53 105.6) (end 53 125.6) (layer "Edge.Cuts") (width 0.1))
   (gr_line (start 50 22.599999) (end 53 22.599999) (layer "Edge.Cuts") (width 0.1))
@@
   (gr_line (start 50 -2.599999) (end 53 -2.599999) (layer "Edge.Cuts") (width 0.1))
   (gr_line (start 50 80.4) (end 50 100.4) (layer "Edge.Cuts") (width 0.1))
-  (gr_circle (center 0 0) (end 3.25 0) (layer "Edge.Cuts") (width 0.1) (fill none))
   (gr_line (start 125.6 50) (end 125.6 53) (layer "Edge.Cuts") (width 0.1))
   (gr_line (start 50 130.799999) (end 50 153) (layer "Edge.Cuts") (width 0.1))
   (gr_line (start 53 -50) (end 153 -50) (layer "Edge.Cuts") (width 0.1))
   (gr_line (start 2.6 50) (end 22.599999 50) (layer "Edge.Cuts") (width 0.1))
+  (gr_circle (center 103 0) (end 106.25 0) (layer "Edge.Cuts") (width 0.1) (fill none))
   (gr_line (start -22.599999 50) (end -2.599999 50) (layer "Edge.Cuts") (width 0.1))
   (gr_line (start 27.799999 50) (end 27.799999 53) (layer "Edge.Cuts") (width 0.1))
@@
   (segment (start -7.6354 145.9046) (end -5.08 148.46) (width 0.9) (layer "F.Cu") (net 3))
   (segment (start 145.9003 15.5277) (end 145.1954 14.8228) (width 0.9) (layer "F.Cu") (net 3))
+  (segment (start -41.7 -28.5164) (end -41.558 -28.5164) (width 0.9) (layer "F.Cu") (net 3))
   (segment (start 87.8497 42.9046) (end 95.3646 42.9046) (width 0.9) (layer "F.Cu") (net 3))
   (segment (start 57.54 97.92) (end 59.0403 97.92) (width 0.9) (layer "F.Cu") (net 3))
@@
   (segment (start 134.7 11.8497) (end 130.4434 11.8497) (width 0.9) (layer "F.Cu") (net 3))
   (segment (start 12.584 140.8709) (end 14.8582 138.5967) (width 0.9) (layer "F.Cu") (net 3))
+  (segment (start -9.6686 -35.636) (end 7.6749 -35.636) (width 0.9) (layer "F.Cu") (net 3))
   (segment (start 42.357 94.817) (end 41.7 94.817) (width 0.9) (layer "F.Cu") (net 3))
   (segment (start 71.3 -13.5) (end 71.3 -11.8497) (width 0.9) (layer "F.Cu") (net 3))
@@
   (segment (start 144.7 132.3415) (end 144.7 133.1667) (width 0.9) (layer "F.Cu") (net 3))
   (segment (start 145.9003 130.3161) (end 145.9003 118.5277) (width 0.9) (layer "F.Cu") (net 3))
-  (segment (start -9.6686 -35.636) (end 7.6749 -35.636) (width 0.9) (layer "F.Cu") (net 3))
   (segment (start -5.08 148.46) (end -5.08 151) (width 0.9) (layer "F.Cu") (net 3))
   (segment (start 125.9706 127.4398) (end 93.9034 127.4398) (width 0.9) (layer "F.Cu") (net 3))
@@
   (segment (start 31.7 11.8497) (end 27.4434 11.8497) (width 0.9) (layer "F.Cu") (net 3))
   (segment (start 148.46 97.92) (end 149.4997 97.92) (width 0.9) (layer "F.Cu") (net 3))
-  (segment (start -41.7 -28.5164) (end -41.558 -28.5164) (width 0.9) (layer "F.Cu") (net 3))
   (segment (start 42.9003 118.5277) (end 42.1954 117.8228) (width 0.9) (layer "F.Cu") (net 3))
   (segment (start 118.5379 -42.9003) (end 130.3161 -42.9003) (width 0.9) (layer "F.Cu") (net 3))
